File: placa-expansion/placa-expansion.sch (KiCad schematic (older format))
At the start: 12 parts, among them J1 PBD-26, P1 BATT, P2 CONN_3PI, P3 PWR_HUB, P4 PWR_3pi, U1 PTN78020

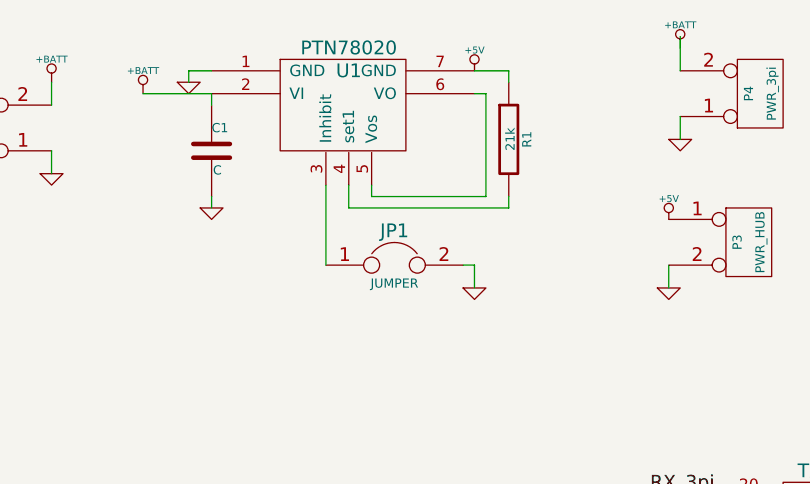
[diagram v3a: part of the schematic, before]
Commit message: Revisamos el esquematico.
Faltan agregar los sensores.
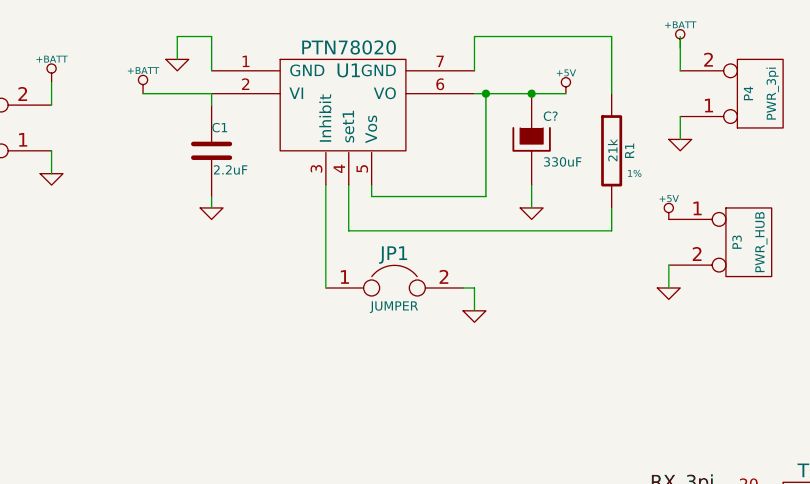
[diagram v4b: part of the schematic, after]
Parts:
- added C?: 330uF, ~, symbol CAPAPOL
- C1: value C -> 2.2uF
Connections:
- net +5V: now also U1.5 (Vos), U1.6 (VO), C?.1; no longer R1.1, U1.7 (GND)
- net GND: now also C?.2
- new net: R1.1, U1.7 (GND)
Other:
- moved on the sheet: JP1, R1
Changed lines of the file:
@@
-EESchema Schematic File Version 2  date vie 03 may 2013 22:07:03 ART
+EESchema Schematic File Version 2  date vie 10 may 2013 20:36:57 ART
 LIBS:power
 LIBS:device
@@
 Sheet 1 1
 Title "Expansión para el 3pi - Raspberry Pi"
-Date "4 may 2013"
+Date "10 may 2013"
 Rev "0.1"
 Comp "Club de Robótica FIUBA"
@@
 P 2600 1300
 F 0 "C1" H 2600 1400 40  0000 L CNN
-F 1 "C" H 2606 1215 40  0000 L CNN
+F 1 "2.2uF" H 2606 1215 40  0000 L CNN
 F 2 "~" H 2638 1150 30  0000 C CNN
-F 3 "~" H 2600 1300 60  0000 C CNN
+F 3 "Cerámico" H 2600 1300 60  0001 C CNN
 	1    2600 1300
 	1    0    0    -1
@@
 L GND #PWR6
 U 1 1 5184557F
-P 2500 1000
-F 0 "#PWR6" H 2500 1000 30  0001 C CNN
-F 1 "GND" H 2500 930 30  0001 C CNN
-F 2 "" H 2500 1000 60  0000 C CNN
-F 3 "" H 2500 1000 60  0000 C CNN
-	1    2500 1000
+P 2450 900
+F 0 "#PWR6" H 2450 900 30  0001 C CNN
+F 1 "GND" H 2450 830 30  0001 C CNN
+F 2 "" H 2450 900 60  0000 C CNN
+F 3 "" H 2450 900 60  0000 C CNN
+	1    2450 900
 	1    0    0    -1
 $EndComp
@@
 L JUMPER JP1
 U 1 1 518455E3
-P 3400 1800
-F 0 "JP1" H 3400 1950 60  0000 C CNN
-F 1 "JUMPER" H 3400 1720 40  0000 C CNN
-F 2 "~" H 3400 1800 60  0000 C CNN
-F 3 "~" H 3400 1800 60  0000 C CNN
-	1    3400 1800
+P 3400 1900
+F 0 "JP1" H 3400 2050 60  0000 C CNN
+F 1 "JUMPER" H 3400 1820 40  0000 C CNN
+F 2 "~" H 3400 1900 60  0000 C CNN
+F 3 "~" H 3400 1900 60  0000 C CNN
+	1    3400 1900
 	1    0    0    -1
 $EndComp
@@
 L GND #PWR11
 U 1 1 51845607
-P 3750 1900
-F 0 "#PWR11" H 3750 1900 30  0001 C CNN
-F 1 "GND" H 3750 1830 30  0001 C CNN
-F 2 "" H 3750 1900 60  0000 C CNN
-F 3 "" H 3750 1900 60  0000 C CNN
-	1    3750 1900
+P 3750 2000
+F 0 "#PWR11" H 3750 2000 30  0001 C CNN
+F 1 "GND" H 3750 1930 30  0001 C CNN
+F 2 "" H 3750 2000 60  0000 C CNN
+F 3 "" H 3750 2000 60  0000 C CNN
+	1    3750 2000
 	1    0    0    -1
 $EndComp
@@
 	3800 1500 3800 1050
 Wire Wire Line
-	3800 1050 3750 1050
+	3750 1050 4150 1050
 $Comp
 L R R1
 U 1 1 518456B1
-P 3900 1250
-F 0 "R1" V 3980 1250 40  0000 C CNN
-F 1 "21k" V 3907 1251 40  0000 C CNN
-F 2 "~" V 3830 1250 30  0000 C CNN
-F 3 "~" H 3900 1250 30  0000 C CNN
-	1    3900 1250
-	1    0    0    -1
-$EndComp
-Wire Wire Line
-	3200 1450 3200 1550
-Wire Wire Line
-	3200 1550 3900 1550
-Wire Wire Line
-	3900 1550 3900 1500
-Wire Wire Line
-	3900 1000 3900 950
-Wire Wire Line
-	3900 950  3750 950
-Wire Wire Line
-	3100 1450 3100 1800
-Wire Wire Line
-	3700 1800 3750 1800
-Wire Wire Line
-	3750 1800 3750 1900
-Wire Wire Line
-	2600 950  2500 950
-Wire Wire Line
-	2500 950  2500 1000
+P 4350 1300
+F 0 "R1" V 4430 1300 40  0000 C CNN
+F 1 "21k" V 4357 1301 40  0000 C CNN
+F 2 "~" V 4280 1300 30  0000 C CNN
+F 3 "1%" H 4450 1200 30  0000 C CNN
+	1    4350 1300
+	1    0    0    -1
+$EndComp
+Wire Wire Line
+	3200 1450 3200 1650
+Wire Wire Line
+	3100 1450 3100 1900
+Wire Wire Line
+	3700 1900 3750 1900
+Wire Wire Line
+	3750 1900 3750 2000
+Wire Wire Line
+	2450 800  2600 800
+Wire Wire Line
+	2450 800  2450 900
 Wire Wire Line
 	2600 1050 2600 1100
@@
 L +5V #PWR10
 U 1 1 518458AE
-P 3750 950
-F 0 "#PWR10" H 3750 1040 20  0001 C CNN
-F 1 "+5V" H 3750 1040 30  0000 C CNN
-F 2 "" H 3750 950 60  0000 C CNN
-F 3 "" H 3750 950 60  0000 C CNN
-	1    3750 950
+P 4150 1050
+F 0 "#PWR10" H 4150 1140 20  0001 C CNN
+F 1 "+5V" H 4150 1140 30  0000 C CNN
+F 2 "" H 4150 1050 60  0000 C CNN
+F 3 "" H 4150 1050 60  0000 C CNN
+	1    4150 1050
 	1    0    0    -1
 $EndComp
@@
 NoConn ~ 9000 3650
 NoConn ~ 9000 3450
+Wire Wire Line
+	2600 800  2600 950
+$Comp
+L CAPAPOL C?
+U 1 1 518D74D8
+P 4000 1250
+F 0 "C?" H 4050 1350 40  0000 L CNN
+F 1 "330uF" H 4050 1150 40  0000 L CNN
+F 2 "~" H 4100 1100 30  0000 C CNN
+F 3 "~" H 4000 1250 300 0000 C CNN
+	1    4000 1250
+	1    0    0    -1
+$EndComp
+Connection ~ 3800 1050
+$Comp
+L GND #PWR?
+U 1 1 518D7578
+P 4000 1550
+F 0 "#PWR?" H 4000 1550 30  0001 C CNN
+F 1 "GND" H 4000 1480 30  0001 C CNN
+F 2 "" H 4000 1550 60  0000 C CNN
+F 3 "" H 4000 1550 60  0000 C CNN
+	1    4000 1550
+	1    0    0    -1
+$EndComp
+Wire Wire Line
+	4000 1450 4000 1550
+Wire Wire Line
+	3200 1650 4350 1650
+Wire Wire Line
+	4350 800  4350 1050
+Wire Wire Line
+	4350 1650 4350 1550
+Connection ~ 4000 1050
+Wire Wire Line
+	3750 950  3750 800
+Wire Wire Line
+	3750 800  4350 800
 $EndSCHEMATC

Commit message: Terminamos el esquemático. Saco dos archivos que no tenian que estar.
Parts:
- added P5, P6, P7, P8: CONN_4, ~, symbol CONN_4
- gave numbers to parts that had none: 1
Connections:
- net labels added: Echo1, Echo2, Echo3, Echo4, Trig
- wire segments 39 -> 52
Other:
- note added: "3pi expansion"
- note added: "Fuente"
- note added: "HC-SR04 UltraSound Pingers"
- moved on the sheet: C1, C2, D1, J1, JP1, P1, P2, P3, P4, R1, R2, U1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
